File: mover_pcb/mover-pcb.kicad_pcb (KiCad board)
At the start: 2 copper layers, 47 x 62.5 mm, 8 parts, among them J1 Conn_01x03_Pin, J2 Conn_01x05_Pin, J3 Conn_01x05_Pin, J4 Conn_01x06_Pin, J5 Conn_01x04_Pin, J6 Conn_01x03_Pin

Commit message: mover_pcb: new revision with voltage divider; update README
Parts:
- added R1: 47k, Resistor_THT:R_Axial_DIN0207_L6.3mm_D2.5mm_P7.62mm_Horizontal, F.Cu at (115.0, 97.9)
- added R2: 10k, Resistor_THT:R_Axial_DIN0207_L6.3mm_D2.5mm_P7.62mm_Horizontal, F.Cu at (115.0, 107.9)
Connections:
- A1 pad 31: unconnected-(A1-GPIO26_ADC0-Pad31) -> Voltage
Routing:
- net Voltage: track 0.00 -> 28.6 mm
- net 12V: track 48.9 -> 65.3 mm
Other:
- board text added: "rev 2"

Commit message: update pcb; progress on controller
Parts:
- removed J5: Conn_01x04_Pin, TerminalBlock_Phoenix:TerminalBlock_Phoenix_MKDS-1,5-4-5.08_1x04_P5.08mm_Horizontal
- removed J6: Conn_01x03_Pin, TerminalBlock_Phoenix:TerminalBlock_Phoenix_MKDS-1,5-3-5.08_1x03_P5.08mm_Horizontal
- removed R1: 47k, Resistor_THT:R_Axial_DIN0207_L6.3mm_D2.5mm_P7.62mm_Horizontal
- removed R2: 10k, Resistor_THT:R_Axial_DIN0207_L6.3mm_D2.5mm_P7.62mm_Horizontal
- added U1: TB6612FNG, TB6612:TB6612FNG_Module, F.Cu at (110.3, 123.0)
- A1: footprint Module:RaspberryPi_Pico_Common_SMD -> Module:RaspberryPi_Pico_Common_THT
- J4: value Conn_01x06_Pin -> Conn_01x02_Pin; footprint Connector_PinHeader_2.54mm:PinHeader_1x06_P2.54mm_Vertical -> TerminalBlock_Phoenix:TerminalBlock_Phoenix_MKDS-1,5-2-5.08_1x02_P5.08mm_Horizontal
- moved A1 25.5 mm to (122.2, 84.1)
- moved J4 18.9 mm to (107.3, 102.1), turned to -90 degrees
- moved G*** 8.73 mm to (131.5, 103.0), turned to -90 degrees
- moved J1 3.73 mm to (116.0, 90.0)
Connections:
- A1 pad 10: unconnected-(A1-GPIO7-Pad10) -> Enable
- A1 pad 14: EnA -> PWMA
- A1 pad 17: EnB -> PWMB
- A1 pad 31: Voltage -> unconnected-(A1-GPIO26_ADC0-Pad31)
- J4 pad 1: EnA -> 12V
- J4 pad 2: IN1 -> GND
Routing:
- net GND: track 16.7 -> 202.6 mm
- net 12V: track 65.3 -> 26.3 mm
- net Voltage: track 28.6 -> 0.00 mm
- net MotorA-: track 61.0 -> 35.9 mm
- net Enable: track 0.00 -> 18.0 mm
- net MotorB-: track 33.4 -> 19.3 mm
- net MotorB+: track 27.3 -> 15.9 mm
- net EnA: track 7.31 -> 0.00 mm
- net EnB: track 7.31 -> 0.00 mm
- net PWMB: track 0.00 -> 7.03 mm
- net PWMA: track 0.00 -> 6.36 mm
- net 5V: track 113.4 -> 110.4 mm, vias 0 -> 1
- net IN1: track 7.31 -> 5.31 mm
- net IN3: track 6.36 -> 7.66 mm
- net IN4: track 6.36 -> 7.66 mm
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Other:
- board size 47 x 62.5 mm -> 44.5 x 62.5 mm
- board text added: "+"
- board text added: "Lights"
- board text removed: "A+"
- board text removed: "B+"
- board text removed: "To L298N Control"
- board text removed: "To L298N Power"
- board text removed: "To Motor"

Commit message: playaround update
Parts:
- added Q2: BS170, Package_TO_SOT_THT:TO-92_Inline, F.Cu at (117.5, 109.5)
- added R1: 10k, Resistor_THT:R_Axial_DIN0204_L3.6mm_D1.6mm_P5.08mm_Horizontal, F.Cu at (118.5, 100.9)
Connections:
- A1 pad 2: unconnected-(A1-GPIO1-Pad2) -> Lights
- J4 pad 2: GND -> Net-(J4-Pin_2)
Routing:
- net Lights: track 0.00 -> 32.1 mm
- net Net-(J4-Pin_2): track 0.00 -> 7.96 mm
- net GND: track 202.6 -> 206.5 mm

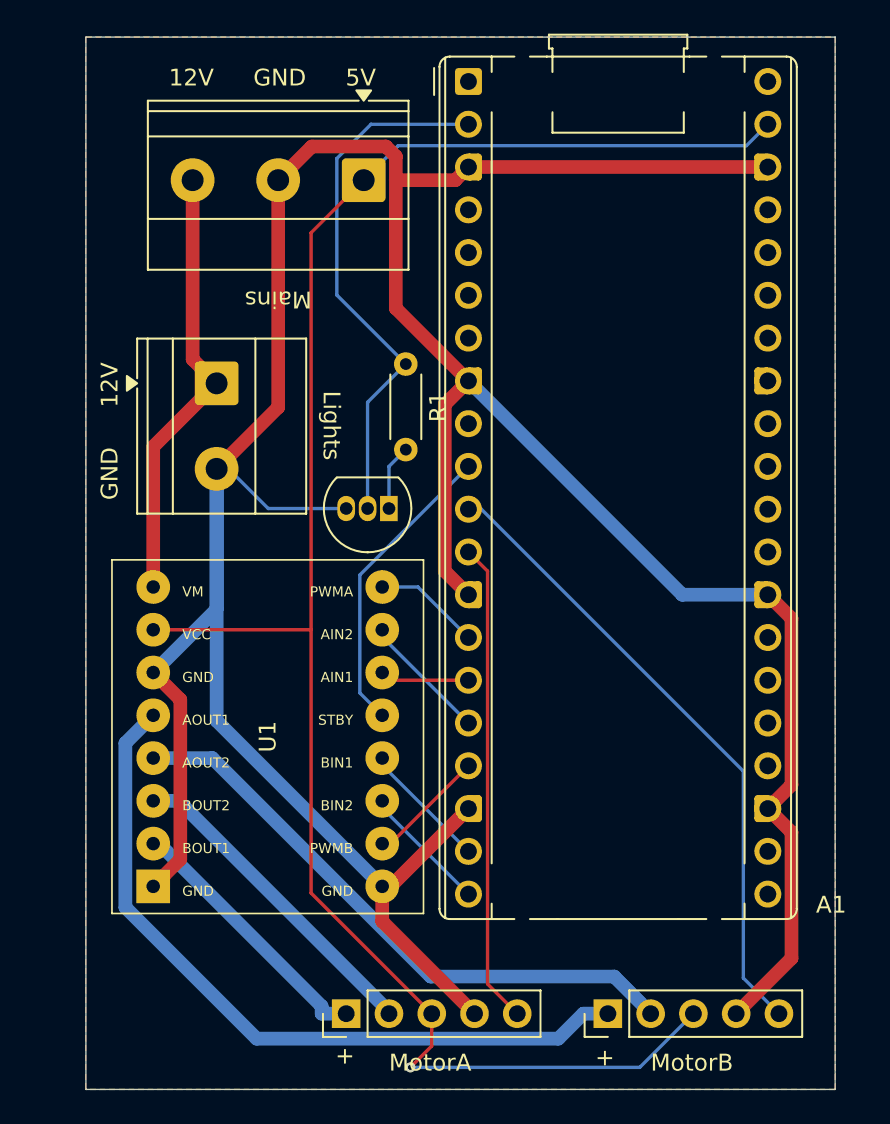
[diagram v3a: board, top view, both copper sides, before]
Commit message: fix TB6612 Module, update pcb
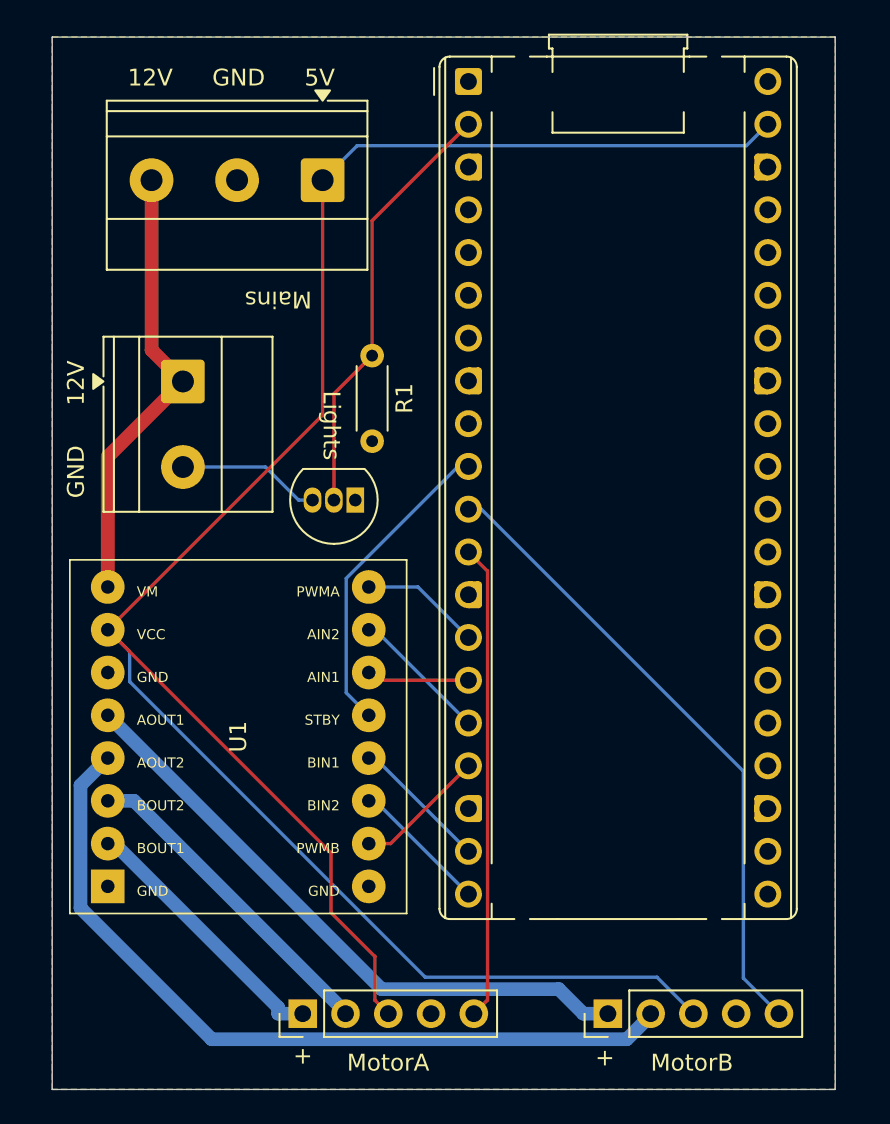
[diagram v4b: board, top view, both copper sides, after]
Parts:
- moved J2 2.58 mm to (112.4, 139.5)
- moved J1 2.44 mm to (113.6, 90.0)
- moved Q2 2.06 mm to (115.5, 109.0)
- moved R1 2.06 mm to (116.5, 100.4)
- moved J4 2.00 mm to (105.3, 102.0)
- moved U1 1.75 mm to (108.5, 123.0)
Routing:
- net GND: track 206.5 -> 0.00 mm
- net 5V: track 110.4 -> 134.8 mm, vias 1 -> 0
- net MotorA-: track 35.9 -> 47.4 mm
- net MotorA+: track 44.6 -> 37.0 mm
- net Lights: track 32.1 -> 25.6 mm
- net PWMB: track 7.03 -> 7.83 mm
- net PWMA: track 6.36 -> 7.16 mm
- net IN1: track 5.31 -> 6.11 mm
- net Enable: track 18.0 -> 18.7 mm
- net IN2: track 7.66 -> 8.21 mm
- net IN3: track 7.66 -> 8.21 mm
- net IN4: track 7.66 -> 8.21 mm
- net Net-(J4-Pin_2): track 7.96 -> 8.51 mm
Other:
- board size 44.5 x 62.5 mm -> 46.5 x 62.5 mm

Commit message: add urdf launch for rviz
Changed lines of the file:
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@@
 	)
 	(gr_text "Lights"
-		(at 113.5 102.5 270)
+		(at 111.25 102.25 270)
 		(layer "F.SilkS")
 		(effects
